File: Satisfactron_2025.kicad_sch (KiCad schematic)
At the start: 128 parts, among them J1 USB-TYPE-C-018, J10 GT-BTP30002-0350B-019B, J11 Conn_01x03, J2 GT-BTP30002-0350B-019B, J3 TF_PUSH, J4 GT-BTP30002-0350B-019B, J5 PZ254V-11-04P_C2691448, J6 Conn_01x06, J7 GT-BTP30002-0350B-019B, J8 GT-BTP30002-0350B-019B, J9 GT-BTP30002-0350B-019B, SW1 MSK-22D18G4_051, SW10 SPVN310101, SW11 SPVN310101, SW12 SPVN310101, SW13 SPVN310101, SW14 SPVN310101, SW15 SPVN310101, SW2 TS-1088-AR02016, SW3 SPVN310101, SW4 SPVN310101, SW5 TS-1088-AR02016, SW6 TS-1088-AR02016, SW7 TS-1088-AR02016, SW8 SPVN310101, SW9 SPVN310101, U1 AMS1117-3.3, U10 WS2811C, U11 WS2811C, U12 WS2811C, U13 WS2811C, U2 TPS82130, U3 ESP32-S3-WROOM-1-N16R8, U4 TSSP77038TR, U5 TSSP77038TR, U6 TSSP77038TR, U7 TSSP77038TR, U8 TSSP77038TR, U9 WS2811C

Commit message: Placement done
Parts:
- removed JP1: SolderJumper_3_Bridged12, symbol Jumper:SolderJumper_3_Bridged12
- removed R10, R11, R12, R14: 10k, Resistor_SMD:R_0603_1608Metric_Pad0.98x0.95mm_HandSolder, symbol Device:R
- added C31: 22uF, Capacitor_SMD:C_0805_2012Metric, symbol Device:C
- added JP2: SolderJumper_3_Bridged12, Jumper:SolderJumper-3_P1.3mm_Bridged12_RoundedPad1.0x1.5mm, symbol Jumper:SolderJumper_3_Bridged12
- added Q1: 2N7002, Package_TO_SOT_SMD:SOT-23_Handsoldering, symbol Transistor_FET:2N7002
- added R10, R11, R43: 4.7k, Resistor_SMD:R_0603_1608Metric, symbol Device:R_Small
- added R12: 10k, Resistor_SMD:R_0603_1608Metric, symbol Device:R_Small
- added R21, R22, R26, R32, R33, R34, R35, R36, R37, R38, R39, R40, R41, R42, R7: 33, Resistor_SMD:R_0603_1608Metric, symbol Device:R_Small
- added U14: TSSP77038TT, Sensor_KSL:Top-view-TSSP770_SMD_TSOP75238TR, symbol Sensor_KSL:TSSP77038TR
- C11, C22, H2, H4, SW11, SW12, SW13, SW14: now not fitted; now left out of the parts list
- C18, C19, C20, C21, C24: footprint (none) -> Capacitor_SMD:C_0603_1608Metric_Pad1.08x0.95mm_HandSolder
- R6: value 68 -> 33
- SW15, U3: now not fitted
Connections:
- net +5P is gone; now on net +5L: C22.1, J11.2 (Pin_2)
- net AU_STATUS is gone; now on net LED_RED: U3.39 (IO1)
- net M1_DIAG/uSW1 is gone; now on net ID2: U3.8 (IO15)
- net M1_DIR is gone; now on net ID1: U3.9 (IO16)
- net M1_STEP is gone; now on net uSW1: U3.25 (IO48)
- net TX_LIDAR is gone; now on net uSW2: U3.24 (IO47)
- net +3.3V: now also C31.1, Q1.1 (G), R10.2, R11.2, R43.2, U14.2 (+VS)
- net +5L: now also R12.2
- net BTN_USER1: now also U3.18 (IO10)
- net BTN_USER2: now also U3.11 (IO18)
- net CARD_DETECT: now also U3.4 (IO4); no longer U3.17 (IO9)
- net GND: now also C31.2, U14.1 (GND), U14.4 (GND)
- net ID1: no longer U3.11 (IO18)
- net ID2: no longer U3.23 (IO21)
- net LED_RED: no longer U3.18 (IO10)
- net RGBLED: now also R5.2, JP2.3 (B), Q1.3 (D), R12.1; no longer R5.1, U3.4 (IO4)
- net SCL: now also R43.1
- net SDA: now also R10.1
- net uSW1: now also SW15.1, SW15.4; no longer SW4.1, SW4.4
- net uSW2: now also SW14.1, SW14.4, SW4.1, SW4.4; no longer SW8.1, SW8.4, SW9.1, SW9.4
- net uSW3: now also SW13.1, SW13.4, SW8.1, SW8.4, U3.23 (IO21); no longer SW10.1, SW10.4, SW11.1, SW11.4, U3.21 (IO13)
- net uSW4: now also SW9.1, SW9.4, U3.22 (IO14); no longer SW13.1, SW13.4
- net uSW5: now also SW10.1, U3.21 (IO13); no longer SW14.1, SW14.4, SW15.1, SW15.4
- net at D5.4 (R), D7.4 (R): now also R33.1; no longer U10.1 (OUTR)
- net at D5.2 (G), D7.2 (G): now also R32.1; no longer U10.2 (OUTG)
- net at D5.1 (B), D7.1 (B): now also R26.1; no longer U10.3 (OUTB)
- net at U10.5 (DO): now also U9.6 (DIN); no longer U11.6 (DIN)
- net at U10.6 (DIN): now also U11.5 (DO); no longer U9.5 (DO)
- net at D1.4 (R), D4.4 (R): now also R7.1; no longer U9.1 (OUTR)
- net at D1.2 (G), D4.2 (G): now also R21.1; no longer U9.2 (OUTG)
- net at D1.1 (B), D4.1 (B): now also R22.1; no longer U9.3 (OUTB)
- net at D13.4 (R), D14.4 (R): now also R42.1; no longer U13.1 (OUTR)
- net at D13.2 (G), D14.2 (G): now also R41.1; no longer U13.2 (OUTG)
- net at D13.1 (B), D14.1 (B): now also R40.1; no longer U13.3 (OUTB)
- net at U13.5 (DO): now also U12.6 (DIN)
- net at U13.6 (DIN): now also R5.1; no longer U12.5 (DO)
- net at D10.4 (R), D9.4 (R): now also R36.1; no longer U11.1 (OUTR)
- net at D10.2 (G), D9.2 (G): now also R35.1; no longer U11.2 (OUTG)
- net at D10.1 (B), D9.1 (B): now also R34.1; no longer U11.3 (OUTB)
- net at D11.4 (R), D12.4 (R): now also R39.1; no longer U12.1 (OUTR)
- net at D11.2 (G), D12.2 (G): now also R38.1; no longer U12.2 (OUTG)
- net at D11.1 (B), D12.1 (B): now also R37.1; no longer U12.3 (OUTB)
- net M2_DIAG/uSW2 renamed IRSENS_F
- net IRSENS_F: now also U14.3 (OUT)
- new net: R36.2, U11.1 (OUTR)
- new net: R33.2, U10.1 (OUTR)
- new net: R32.2, U10.2 (OUTG)
- new net: R26.2, U10.3 (OUTB)
- new net: SW10.4, SW11.1, SW11.4
- new net: R7.2, U9.1 (OUTR)
- new net: R21.2, U9.2 (OUTG)
- new net: R22.2, U9.3 (OUTB)
- new net: R38.2, U12.2 (OUTG)
- new net: R41.2, U13.2 (OUTG)
- new net: R37.2, U12.3 (OUTB)
- new net: JP2.1 (A), Q1.2 (S), R11.1
- new net: R42.2, U13.1 (OUTR)
- new net: R40.2, U13.3 (OUTB)
- new net: R35.2, U11.2 (OUTG)
- new net: R34.2, U11.3 (OUTB)
- new net: U11.6 (DIN), U12.5 (DO)
- new net: R39.2, U12.1 (OUTR)
- new net RGBLED_3V3: JP2.2 (C), U3.17 (IO9)
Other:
- note added: "Demander à Michel de la compta avant d'utiliser SBU1"
- note added: "Front presence top view"
- note added: "JTAGsig don't pull up at boot"
- note added: "Level shifter"
- note added: "Satisfactron ID Select"
- note added: "VDDSPI should not be pulled up"
- note removed: "JTAGsig should be pulldown"
- note removed: "Satisfactron Select"
- note removed: "VDDSPI should be pulldown"
- note removed: "mettre les resistances a chaque bout de la carte"
- moved on the sheet: C12, C13, C21, D1, D11, D14, D5, D9, R17, R5, SW10, SW4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

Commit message: Routing 80%
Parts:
- added J12: LED strip, Connector_PinHeader_2.54mm:PinHeader_1x03_P2.54mm_Vertical, symbol Connector_Generic:Conn_01x03
- J5: now not fitted; now left out of the parts list
- U3: now left out of the parts list
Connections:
- net +5L: now also J12.3 (Pin_3)
- net GND: now also J12.1 (Pin_1)
- net MISO: now also U3.5 (IO5); no longer U3.7 (IO7)
- net MOSI: now also U3.7 (IO7); no longer U3.6 (IO6)
- net SCK: now also U3.6 (IO6); no longer U3.5 (IO5)
- net SCL: now also R10.1, U3.19 (IO11); no longer R43.1, U3.20 (IO12)
- net SDA: now also R43.1, U3.20 (IO12); no longer R10.1, U3.19 (IO11)
- net uSW5: now also SW10.4, SW11.1, SW11.4
- net at U9.5 (DO): now also J12.2 (Pin_2)
- no-connect marks 32 -> 31
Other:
- moved on the sheet: SW10, SW11

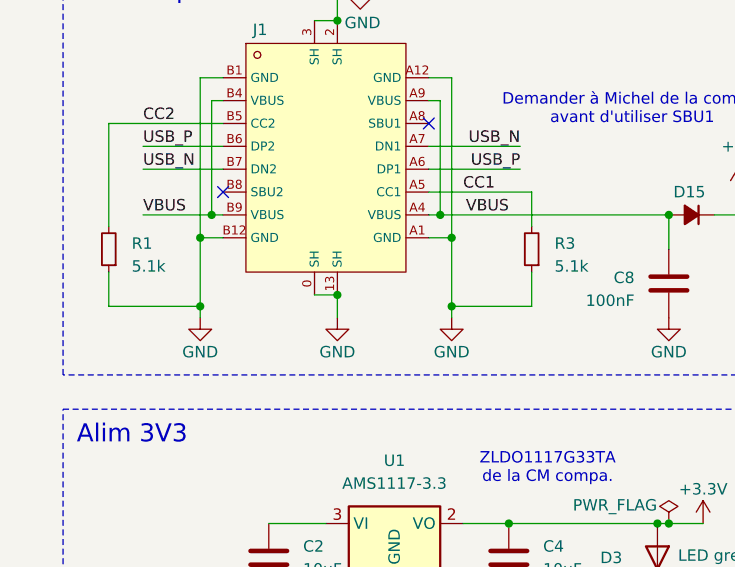
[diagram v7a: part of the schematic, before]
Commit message: Routing done, no zones
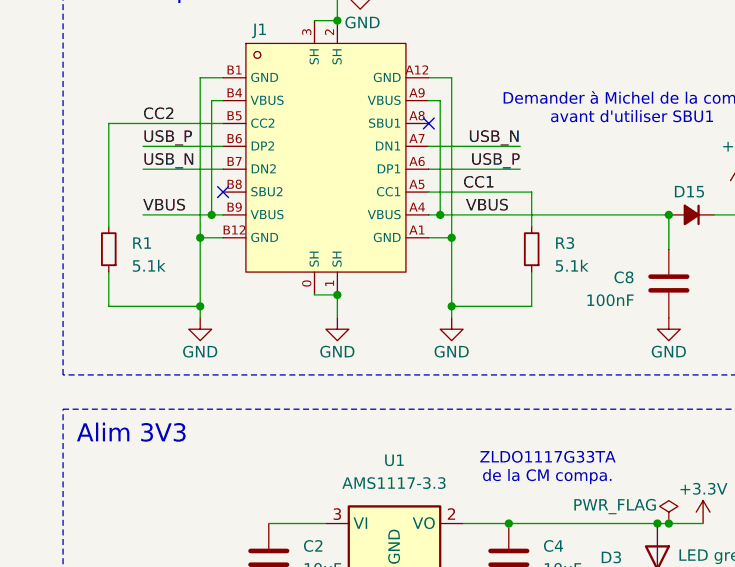
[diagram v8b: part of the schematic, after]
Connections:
- net GND: now also J1.1 (SH); no longer J1.13 (SH)
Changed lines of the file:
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@@
 		(pin "2"
 		)
-		(pin "0"
+		(pin "1"
 		)
 		(pin "A7"
@@
 		(pin "B8"
 		)
-		(pin "13"
+		(pin "0"
 		)
 		(pin "A1"
